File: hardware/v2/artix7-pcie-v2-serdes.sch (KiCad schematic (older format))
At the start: 22 parts, among them J4 USB3_A, J5 USB3_A, U1 XC7A75T-FGG484

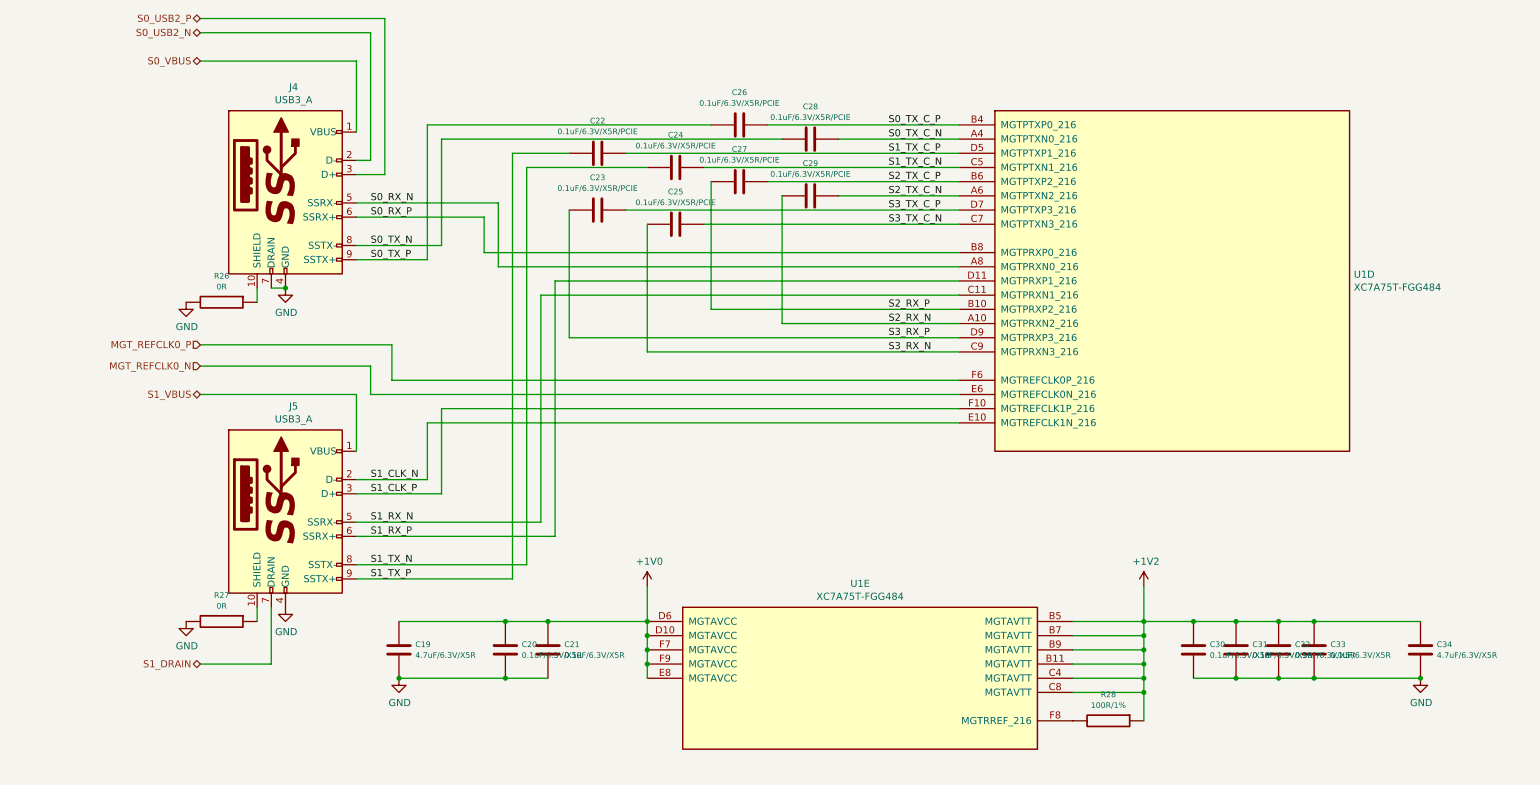
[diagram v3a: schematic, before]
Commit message: v2 pcb/schematic update : drc passing, need to add caps
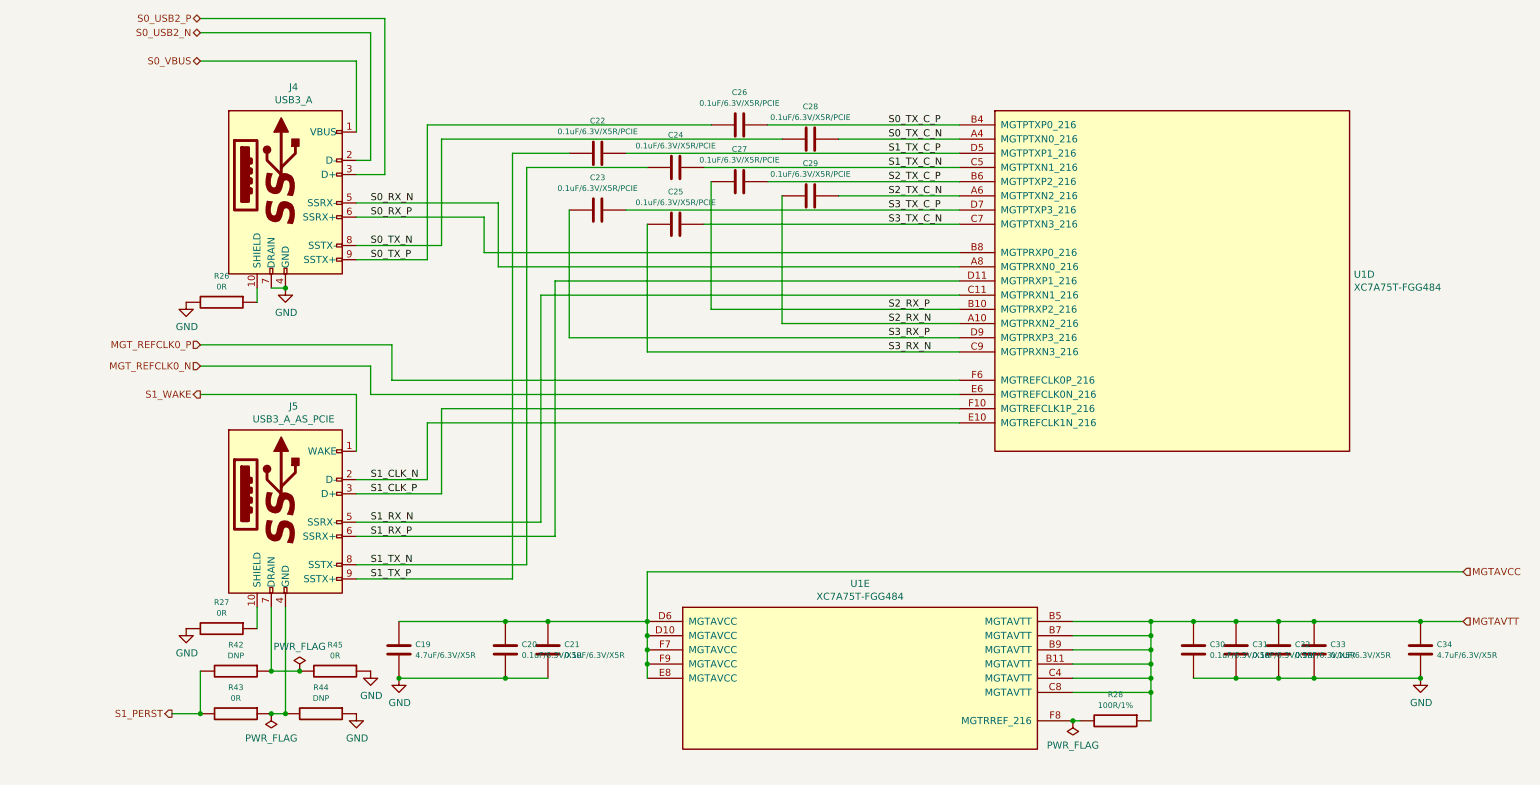
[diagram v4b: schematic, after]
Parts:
- removed J5: USB3_A, tom-connectors:USB3_A_Aliexpress, symbol tom-connectors:USB3_A
- added J5: USB3_A_AS_PCIE, tom-connectors:USB3_A_Aliexpress, symbol tom-connectors:USB3_A_AS_PCIE
- added R42, R44: DNP, tom-passives:C_0402_1005Metric, symbol tom-passives:R
- added R43, R45: 0R, tom-passives:C_0402_1005Metric, symbol tom-passives:R
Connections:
- net GND: now also R44.1, R45.1
- net S1_CLK_N: now also J5.2 (D-)
- net S1_CLK_P: now also J5.3 (D+)
- net S1_RX_N: now also J5.5 (SSRX-)
- net S1_RX_P: now also J5.6 (SSRX+)
- net S1_TX_N: now also J5.8 (SSTX-)
- net S1_TX_P: now also J5.9 (SSTX+)
- net at R27.1: now also J5.10 (SHIELD)
- net +1V0 renamed MGTAVCC
- net +1V2 renamed MGTAVTT
- new net: J5.4 (GND), R43.1, R44.2
- new net: J5.7 (DRAIN), R42.1, R45.2
- new net S1_PERST: R42.2, R43.2
- new net S1_WAKE: J5.1 (WAKE)
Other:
- moved on the sheet: R27, R28
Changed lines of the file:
@@
 EESchema Schematic File Version 4
-LIBS:artix7-pcie-v2-cache
 EELAYER 30 0
 EELAYER END
 $Descr A4 11693 8268
 encoding utf-8
-Sheet 4 7
+Sheet 2 7
 Title ""
 Date ""
@@
 	1    0    0    -1
 $EndComp
-Text HLabel 1900 5600 0    50   BiDi ~ 0
-S1_DRAIN
-Wire Wire Line
-	2400 5600 1900 5600
-Wire Wire Line
-	2400 5200 2400 5600
-Wire Wire Line
-	2300 5200 2300 5300
+Text HLabel 1700 5950 0    50   Output ~ 0
+S1_PERST
+Wire Wire Line
+	2300 5200 2300 5350
 $Comp
 L power:GND #PWR059
 U 1 1 5EAD2F17
-P 1800 5300
-F 0 "#PWR059" H 1800 5050 50  0001 C CNN
-F 1 "GND" H 1805 5127 50  0000 C CNN
-F 2 "" H 1800 5300 50  0001 C CNN
-F 3 "" H 1800 5300 50  0001 C CNN
-	1    1800 5300
+P 1800 5350
+F 0 "#PWR059" H 1800 5100 50  0001 C CNN
+F 1 "GND" H 1805 5177 50  0000 C CNN
+F 2 "" H 1800 5350 50  0001 C CNN
+F 3 "" H 1800 5350 50  0001 C CNN
+	1    1800 5350
 	1    0    0    -1
 $EndComp
@@
 L tom-passives:R R27
 U 1 1 5EAD1FF6
-P 2050 5300
-F 0 "R27" V 1865 5300 40  0000 C CNN
-F 1 "0R" V 1941 5300 40  0000 C CNN
-F 2 "tom-passives:C_0402_1005Metric" V 1980 5300 30  0001 C CNN
-F 3 "" H 2050 5300 30  0001 C CNN
-	1    2050 5300
+P 2050 5350
+F 0 "R27" V 1865 5350 40  0000 C CNN
+F 1 "0R" V 1941 5350 40  0000 C CNN
+F 2 "tom-passives:C_0402_1005Metric" V 1980 5350 30  0001 C CNN
+F 3 "" H 2050 5350 30  0001 C CNN
+	1    2050 5350
 	0    1    1    0
 $EndComp
@@
 L power:GND #PWR061
 U 1 1 5EACBD31
-P 2500 5200
-F 0 "#PWR061" H 2500 4950 50  0001 C CNN
-F 1 "GND" H 2505 5027 50  0000 C CNN
-F 2 "" H 2500 5200 50  0001 C CNN
-F 3 "" H 2500 5200 50  0001 C CNN
-	1    2500 5200
+P 3000 5950
+F 0 "#PWR061" H 3000 5700 50  0001 C CNN
+F 1 "GND" H 3005 5777 50  0000 C CNN
+F 2 "" H 3000 5950 50  0001 C CNN
+F 3 "" H 3000 5950 50  0001 C CNN
+	1    3000 5950
 	1    0    0    -1
 $EndComp
@@
 Wire Wire Line
 	3000 4600 4300 4600
-$Comp
-L tom-connectors:USB3_A J5
-U 1 1 5E9A32AC
-P 2500 4500
-F 0 "J5" H 2557 5217 50  0000 C CNN
-F 1 "USB3_A" H 2557 5126 50  0000 C CNN
-F 2 "tom-connectors:USB3_A_Aliexpress" H 2650 4600 50  0001 C CNN
-F 3 "~" H 2650 4600 50  0001 C CNN
-	1    2500 4500
-	1    0    0    -1
-$EndComp
 Wire Wire Line
 	7250 3800 3600 3800
@@
 Text Label 3100 5000 0    50   ~ 0
 S1_TX_P
-Text HLabel 1900 1350 0    50   BiDi ~ 0
-S0_VBUS
 Wire Wire Line
 	3000 1850 3000 1350
 Wire Wire Line
 	3000 1350 1900 1350
-Text HLabel 1900 3700 0    50   BiDi ~ 0
-S1_VBUS
+Text HLabel 1900 3700 0    50   Output ~ 0
+S1_WAKE
 Wire Wire Line
 	3000 4100 3000 3700
@@
 L tom-passives:R R28
 U 1 1 5EB72E9F
-P 8300 6000
-F 0 "R28" V 8115 6000 40  0000 C CNN
-F 1 "100R/1%" V 8191 6000 40  0000 C CNN
-F 2 "tom-passives:C_0402_1005Metric" V 8230 6000 30  0001 C CNN
-F 3 "" H 8300 6000 30  0001 C CNN
-	1    8300 6000
-	0    1    1    0
-$EndComp
-$Comp
-L power:+1V2 #PWR064
-U 1 1 5EB7A45C
-P 8550 5050
-F 0 "#PWR064" H 8550 4900 50  0001 C CNN
-F 1 "+1V2" H 8565 5223 50  0000 C CNN
-F 2 "" H 8550 5050 50  0001 C CNN
-F 3 "" H 8550 5050 50  0001 C CNN
-	1    8550 5050
-	1    0    0    -1
-$EndComp
-Wire Wire Line
-	8050 5300 8550 5300
-Wire Wire Line
-	8550 5050 8550 5300
-Connection ~ 8550 5300
-Wire Wire Line
-	8550 5300 8550 5400
-Wire Wire Line
-	8050 5400 8550 5400
-Connection ~ 8550 5400
-Wire Wire Line
-	8050 5500 8550 5500
-Wire Wire Line
-	8550 5400 8550 5500
-Connection ~ 8550 5500
-Wire Wire Line
-	8550 5500 8550 5600
-Wire Wire Line
-	8050 5600 8550 5600
-Connection ~ 8550 5600
-Wire Wire Line
-	8550 5600 8550 5700
-Wire Wire Line
-	8050 5700 8550 5700
-Connection ~ 8550 5700
-Wire Wire Line
-	8550 5700 8550 5800
-Wire Wire Line
-	8050 5800 8550 5800
-Connection ~ 8550 5800
-Wire Wire Line
-	8550 5800 8550 6000
+P 8350 6000
+F 0 "R28" V 8165 6000 40  0000 C CNN
+F 1 "100R/1%" V 8241 6000 40  0000 C CNN
+F 2 "tom-passives:C_0402_1005Metric" V 8280 6000 30  0001 C CNN
+F 3 "" H 8350 6000 30  0001 C CNN
+	1    8350 6000
+	0    1    1    0
+$EndComp
+Wire Wire Line
+	8050 5300 8600 5300
+Connection ~ 8600 5300
+Wire Wire Line
+	8600 5300 8600 5400
+Wire Wire Line
+	8050 5400 8600 5400
+Connection ~ 8600 5400
+Wire Wire Line
+	8050 5500 8600 5500
+Wire Wire Line
+	8600 5400 8600 5500
+Connection ~ 8600 5500
+Wire Wire Line
+	8600 5500 8600 5600
+Wire Wire Line
+	8050 5600 8600 5600
+Connection ~ 8600 5600
+Wire Wire Line
+	8600 5600 8600 5700
+Wire Wire Line
+	8050 5700 8600 5700
+Connection ~ 8600 5700
+Wire Wire Line
+	8600 5700 8600 5800
+Wire Wire Line
+	8050 5800 8600 5800
 $Comp
 L tom-passives:C C30
@@
 $EndComp
 Wire Wire Line
-	8550 5300 8900 5300
+	8600 5300 8900 5300
 Connection ~ 8900 5300
 Wire Wire Line
@@
 Wire Wire Line
 	8900 5700 9200 5700
-$Comp
-L power:+1V0 #PWR063
-U 1 1 5EBF7D68
-P 5050 5050
-F 0 "#PWR063" H 5050 4900 50  0001 C CNN
-F 1 "+1V0" H 5065 5223 50  0000 C CNN
-F 2 "" H 5050 5050 50  0001 C CNN
-F 3 "" H 5050 5050 50  0001 C CNN
-	1    5050 5050
-	1    0    0    -1
-$EndComp
 Wire Wire Line
 	5050 5700 5050 5600
 Connection ~ 5050 5300
-Wire Wire Line
-	5050 5300 5050 5050
 Connection ~ 5050 5400
 Wire Wire Line
@@
 Text HLabel 1900 3350 0    50   Input ~ 0
 MGT_REFCLK0_P
+Text HLabel 10800 5300 2    50   Input ~ 0
+MGTAVTT
+Wire Wire Line
+	10800 5300 10500 5300
+Connection ~ 10500 5300
+Text HLabel 10800 4950 2    50   Input ~ 0
+MGTAVCC
+Wire Wire Line
+	10800 4950 5050 4950
+Wire Wire Line
+	5050 4950 5050 5300
+Wire Wire Line
+	8600 5800 8600 6000
+Connection ~ 8600 5800
+Wire Wire Line
+	8100 6000 8050 6000
+$Comp
+L power:PWR_FLAG #FLG0112
+U 1 1 5EE50010
+P 8050 6000
+F 0 "#FLG0112" H 8050 6075 50  0001 C CNN
+F 1 "PWR_FLAG" H 8050 6173 50  0000 C CNN
+F 2 "" H 8050 6000 50  0001 C CNN
+F 3 "~" H 8050 6000 50  0001 C CNN
+	1    8050 6000
+	-1   0    0    1
+$EndComp
+Connection ~ 8050 6000
+Text HLabel 1900 1350 0    50   BiDi ~ 0
+S0_VBUS
+$Comp
+L tom-connectors:USB3_A_AS_PCIE J5
+U 1 1 5EEEB708
+P 2500 4500
+F 0 "J5" H 2557 5217 50  0000 C CNN
+F 1 "USB3_A_AS_PCIE" H 2557 5126 50  0000 C CNN
+F 2 "tom-connectors:USB3_A_Aliexpress" H 2650 4600 50  0001 C CNN
+F 3 "~" H 2650 4600 50  0001 C CNN
+	1    2500 4500
+	1    0    0    -1
+$EndComp
+$Comp
+L tom-passives:R R44
+U 1 1 5F029E9A
+P 2750 5950
+F 0 "R44" V 2565 5950 40  0000 C CNN
+F 1 "DNP" V 2641 5950 40  0000 C CNN
+F 2 "tom-passives:C_0402_1005Metric" V 2680 5950 30  0001 C CNN
+F 3 "" H 2750 5950 30  0001 C CNN
+	1    2750 5950
+	0    1    1    0
+$EndComp
+$Comp
+L tom-passives:R R43
+U 1 1 5F02A201
+P 2150 5950
+F 0 "R43" V 1965 5950 40  0000 C CNN
+F 1 "0R" V 2041 5950 40  0000 C CNN
+F 2 "tom-passives:C_0402_1005Metric" V 2080 5950 30  0001 C CNN
+F 3 "" H 2150 5950 30  0001 C CNN
+	1    2150 5950
+	0    1    1    0
+$EndComp
+Wire Wire Line
+	2500 5200 2500 5950
+Wire Wire Line
+	2500 5950 2400 5950
+Connection ~ 2500 5950
+Wire Wire Line
+	1700 5950 1900 5950
+$Comp
+L tom-passives:R R42
+U 1 1 5F0598E8
+P 2150 5650
+F 0 "R42" V 1965 5650 40  0000 C CNN
+F 1 "DNP" V 2041 5650 40  0000 C CNN
+F 2 "tom-passives:C_0402_1005Metric" V 2080 5650 30  0001 C CNN
+F 3 "" H 2150 5650 30  0001 C CNN
+	1    2150 5650
+	0    1    1    0
+$EndComp
+Wire Wire Line
+	1900 5650 1900 5950
+Connection ~ 1900 5950
+Wire Wire Line
+	2400 5200 2400 5650
+$Comp
+L tom-passives:R R45
+U 1 1 5F07398D
+P 2850 5650
+F 0 "R45" V 2665 5650 40  0000 C CNN
+F 1 "0R" V 2741 5650 40  0000 C CNN
+F 2 "tom-passives:C_0402_1005Metric" V 2780 5650 30  0001 C CNN
+F 3 "" H 2850 5650 30  0001 C CNN
+	1    2850 5650
+	0    1    1    0
+$EndComp
+$Comp
+L power:GND #PWR035
+U 1 1 5F073E12
+P 3100 5650
+F 0 "#PWR035" H 3100 5400 50  0001 C CNN
+F 1 "GND" H 3105 5477 50  0000 C CNN
+F 2 "" H 3100 5650 50  0001 C CNN
+F 3 "" H 3100 5650 50  0001 C CNN
+	1    3100 5650
+	1    0    0    -1
+$EndComp
+Wire Wire Line
+	2600 5650 2400 5650
+Connection ~ 2400 5650
+$Comp
+L power:PWR_FLAG #FLG0114
+U 1 1 5F118316
+P 2600 5650
+F 0 "#FLG0114" H 2600 5725 50  0001 C CNN
+F 1 "PWR_FLAG" H 2600 5823 50  0000 C CNN
+F 2 "" H 2600 5650 50  0001 C CNN
+F 3 "~" H 2600 5650 50  0001 C CNN
+	1    2600 5650
+	1    0    0    -1
+$EndComp
+Connection ~ 2600 5650
+$Comp
+L power:PWR_FLAG #FLG0115
+U 1 1 5F11842A
+P 2400 5950
+F 0 "#FLG0115" H 2400 6025 50  0001 C CNN
+F 1 "PWR_FLAG" H 2400 6123 50  0000 C CNN
+F 2 "" H 2400 5950 50  0001 C CNN
+F 3 "~" H 2400 5950 50  0001 C CNN
+	1    2400 5950
+	-1   0    0    1
+$EndComp
+Connection ~ 2400 5950
 $EndSCHEMATC

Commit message: v2 hardware: pcb progress commit, 155 unrouted
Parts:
- removed C23, C25, C27, C29: 0.1uF/6.3V/X5R/PCIE, tom-passives:C_0402_1005Metric, symbol tom-passives:C
- removed C31: 0.1uF/6.3V/X5R, tom-passives:C_0402_1005Metric, symbol tom-passives:C
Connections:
- net S2_RX_N is gone; now on net GND: U1.A10 (MGTPRXN2_216)
- net S2_RX_P is gone; now on net GND: U1.B10 (MGTPRXP2_216)
- net GND: now also U1.C11 (MGTPRXN1_216), U1.D11 (MGTPRXP1_216)
- net MGTAVTT: now also R28.2; no longer R28.1
- net S3_RX_N: now also J5.5 (SSRX-)
- net S3_RX_P: now also J5.6 (SSRX+)
- net S3_TX_C_N: now also C24.1
- net S3_TX_C_P: now also C22.1
- net MGTRREF: now reaches U1.F8 (MGTRREF_216)
- net MGTRREF: now also R28.1; no longer R28.2
- net S1_CLK_N renamed S3_CLK_N
- net S1_CLK_P renamed S3_CLK_P
- net S1_PERST renamed S3_PERST
- removed net S1_RX_N: J5.5 (SSRX-), U1.C11 (MGTPRXN1_216)
- removed net S1_RX_P: J5.6 (SSRX+), U1.D11 (MGTPRXP1_216)
- net S1_TX_C_N: no longer names the net of U1.C5 (MGTPTXN1_216)
- net S1_TX_C_N: no longer C24.1
- net S1_TX_C_P: no longer names the net of U1.D5 (MGTPTXP1_216)
- net S1_TX_C_P: no longer C22.1
- net S1_TX_N renamed S3_TX_N
- net S1_TX_P renamed S3_TX_P
- net S1_WAKE renamed S3_WAKE
- net S2_TX_C_N: no longer names the net of U1.A6 (MGTPTXN2_216)
- net S2_TX_C_P: no longer names the net of U1.B6 (MGTPTXP2_216)
- no-connect marks 0 -> 4
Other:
- moved on the sheet: C22, C24, C32, C33, C34

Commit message: v2 pcb/schematic progress commit, all tough signals routed out
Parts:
- added C47, C48: 0.1uF/6.3V/X5R/PCIE, tom-passives:C_0402_1005Metric, symbol tom-passives:C
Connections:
- net GND: now also U1.C9 (MGTPRXN3_216), U1.D9 (MGTPRXP3_216); no longer U1.A10 (MGTPRXN2_216), U1.B10 (MGTPRXP2_216)
- net S2_TX_C_N: now reaches U1.A6 (MGTPTXN2_216)
- net S2_TX_C_N: now also C24.1
- net S2_TX_C_P: now reaches U1.B6 (MGTPTXP2_216)
- net S2_TX_C_P: now also C22.1
- net S2_GND: now reaches J5.4 (GND), R43.1, R44.2
- net S2_DRAIN: now reaches J5.7 (DRAIN), R42.1, R45.2
- net S3_CLK_N renamed MGTREFCLK1_C_N
- net MGTREFCLK1_C_N: now also C48.2; no longer U1.E10 (MGTREFCLK1N_216)
- net S3_CLK_P renamed MGTREFCLK1_C_P
- net MGTREFCLK1_C_P: now also C47.2; no longer U1.F10 (MGTREFCLK1P_216)
- net S3_PERST renamed S2_PERST
- net S3_RX_N renamed S2_RX_N
- net S2_RX_N: now also U1.A10 (MGTPRXN2_216); no longer U1.C9 (MGTPRXN3_216)
- net S3_RX_P renamed S2_RX_P
- net S2_RX_P: now also U1.B10 (MGTPRXP2_216); no longer U1.D9 (MGTPRXP3_216)
- net S3_TX_C_N: no longer names the net of U1.C7 (MGTPTXN3_216)
- net S3_TX_C_N: no longer C24.1
- net S3_TX_C_P: no longer names the net of U1.D7 (MGTPTXP3_216)
- net S3_TX_C_P: no longer C22.1
- net S3_TX_N renamed S2_TX_N
- net S3_TX_P renamed S2_TX_P
- net S3_WAKE renamed S2_WAKE
- new net MGTREFCLK1_N: C48.1, U1.E10 (MGTREFCLK1N_216)
- new net MGTREFCLK1_P: C47.1, U1.F10 (MGTREFCLK1P_216)
- no-connect marks 4 -> 2
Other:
- moved on the sheet: C22, C24
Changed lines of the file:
@@
 Wire Wire Line
 	3900 2700 7250 2700
-Wire Wire Line
-	4300 4600 4300 3400
 Text Label 3100 2350 0    50   ~ 0
 S0_RX_N
@@
 $EndComp
 Text HLabel 1700 5950 0    50   Output ~ 0
-S3_PERST
+S2_PERST
 Wire Wire Line
 	2300 5200 2300 5350
@@
 $EndComp
 Wire Wire Line
-	3000 4300 3500 4300
-Wire Wire Line
-	3000 4400 3600 4400
+	3000 4300 3900 4300
+Wire Wire Line
+	3000 4400 4000 4400
 Text Label 3100 4700 0    50   ~ 0
-S3_RX_P
+S2_RX_P
 Text Label 3100 4600 0    50   ~ 0
-S3_RX_N
+S2_RX_N
 Text Label 3100 4400 0    50   ~ 0
-S3_CLK_P
+MGTREFCLK1_C_P
 Text Label 3100 4300 0    50   ~ 0
-S3_CLK_N
-Wire Wire Line
-	3500 3900 7250 3900
-Wire Wire Line
-	3500 4300 3500 3900
-Wire Wire Line
-	4400 4700 3000 4700
+MGTREFCLK1_C_N
+Wire Wire Line
+	3900 3900 5450 3900
+Wire Wire Line
+	3900 4300 3900 3900
 Wire Wire Line
 	3000 4600 4300 4600
 Wire Wire Line
-	7250 3800 3600 3800
-Wire Wire Line
-	3600 3800 3600 4400
+	7250 3800 5350 3800
+Wire Wire Line
+	4000 3800 4000 4400
 Text Label 3100 4900 0    50   ~ 0
-S3_TX_N
+S2_TX_N
 Text Label 3100 5000 0    50   ~ 0
-S3_TX_P
+S2_TX_P
 Wire Wire Line
 	3000 1850 3000 1350
@@
 	3000 1350 1900 1350
 Text HLabel 1900 3700 0    50   Output ~ 0
-S3_WAKE
+S2_WAKE
 Wire Wire Line
 	3000 4100 3000 3700
@@
 L tom-passives:C C22
 U 1 1 5E746FE8
-P 4700 2400
-F 0 "C22" V 4471 2400 40  0000 C CNN
-F 1 "0.1uF/6.3V/X5R/PCIE" V 4547 2400 40  0000 C CNN
-F 2 "tom-passives:C_0402_1005Metric" H 4738 2250 30  0001 C CNN
-F 3 "" H 4700 2400 60  0001 C CNN
-	1    4700 2400
+P 4700 2200
+F 0 "C22" V 4471 2200 40  0000 C CNN
+F 1 "0.1uF/6.3V/X5R/PCIE" V 4547 2200 40  0000 C CNN
+F 2 "tom-passives:C_0402_1005Metric" H 4738 2050 30  0001 C CNN
+F 3 "" H 4700 2200 60  0001 C CNN
+	1    4700 2200
 	0    1    1    0
 $EndComp
@@
 L tom-passives:C C24
 U 1 1 5E7489FC
-P 5200 2500
-F 0 "C24" V 4971 2500 40  0000 C CNN
-F 1 "0.1uF/6.3V/X5R/PCIE" V 5047 2500 40  0000 C CNN
-F 2 "tom-passives:C_0402_1005Metric" H 5238 2350 30  0001 C CNN
-F 3 "" H 5200 2500 60  0001 C CNN
-	1    5200 2500
-	0    1    1    0
-$EndComp
-Wire Wire Line
-	4400 3300 4400 4700
+P 5200 2300
+F 0 "C24" V 4971 2300 40  0000 C CNN
+F 1 "0.1uF/6.3V/X5R/PCIE" V 5047 2300 40  0000 C CNN
+F 2 "tom-passives:C_0402_1005Metric" H 5238 2150 30  0001 C CNN
+F 3 "" H 5200 2300 60  0001 C CNN
+	1    5200 2300
+	0    1    1    0
+$EndComp
 Wire Wire Line
 	4000 2800 4000 2350
@@
 	4000 2800 7250 2800
 Wire Wire Line
-	4500 2400 4100 2400
-Wire Wire Line
-	4100 2400 4100 5000
+	4500 2200 4100 2200
 Wire Wire Line
 	4100 5000 3000 5000
@@
 	3000 4900 4200 4900
 Wire Wire Line
-	4200 4900 4200 2500
-Wire Wire Line
-	4200 2500 5000 2500
+	4200 2300 5000 2300
 Wire Wire Line
 	2400 2950 2500 2950
@@
 Text Label 6750 1800 0    50   ~ 0
 S0_TX_C_P
-Text Label 6750 2400 0    50   ~ 0
-S3_TX_C_P
-Text Label 6750 2500 0    50   ~ 0
-S3_TX_C_N
+Text Label 6750 2200 0    50   ~ 0
+S2_TX_C_P
+Text Label 6750 2300 0    50   ~ 0
+S2_TX_C_N
 Text HLabel 1900 3500 0    50   Input ~ 0
 MGT_REFCLK0_N
@@
 	3100 3700 3100 3500
 Wire Wire Line
-	3100 3500 1900 3500
-Wire Wire Line
 	7250 3600 3250 3600
 Wire Wire Line
 	3250 3600 3250 3350
-Wire Wire Line
-	3250 3350 1900 3350
 Text HLabel 1900 3350 0    50   Input ~ 0
 MGT_REFCLK0_P
@@
 P 2600 5650
 F 0 "#FLG0114" H 2600 5725 50  0001 C CNN
-F 1 "PWR_FLAG" H 2600 5823 50  0000 C CNN
+F 1 "PWR_FLAG" V 2600 5950 50  0000 C CNN
 F 2 "" H 2600 5650 50  0001 C CNN
 F 3 "~" H 2600 5650 50  0001 C CNN
@@
 NoConn ~ 7250 2100
 Wire Wire Line
-	4300 3400 7250 3400
-Wire Wire Line
-	7250 3300 4400 3300
-Wire Wire Line
-	7250 2500 5400 2500
-Wire Wire Line
-	4900 2400 7250 2400
-NoConn ~ 7250 2200
-NoConn ~ 7250 2300
+	4300 3200 7250 3200
+Wire Wire Line
+	7250 3100 4400 3100
+Wire Wire Line
+	7250 2300 5400 2300
+Wire Wire Line
+	4900 2200 7250 2200
 Wire Wire Line
 	7250 2900 7150 2900
@@
 Connection ~ 7150 3000
 Wire Wire Line
-	7150 3000 7150 3100
-Wire Wire Line
-	7150 3100 7250 3100
-Connection ~ 7150 3100
-Wire Wire Line
-	7150 3100 7150 3200
-Wire Wire Line
-	7250 3200 7150 3200
-Connection ~ 7150 3200
-Wire Wire Line
-	7150 3200 7150 4000
-Wire Wire Line
 	8050 6000 8050 6150
 Text Label 8050 6150 0    50   ~ 0
@@
 Wire Wire Line
 	8900 5700 9100 5700
+Text Label 2500 5600 1    50   ~ 0
+S2_GND
+Text Label 2400 5600 1    50   ~ 0
+S2_DRAIN
+Wire Wire Line
+	3100 3500 1900 3500
+Wire Wire Line
+	3250 3350 1900 3350
+$Comp
+L tom-passives:C C48
+U 1 1 5EDACCD3
+P 5650 3900
+F 0 "C48" V 5421 3900 40  0000 C CNN
+F 1 "0.1uF/6.3V/X5R/PCIE" V 5497 3900 40  0000 C CNN
+F 2 "tom-passives:C_0402_1005Metric" H 5688 3750 30  0001 C CNN
+F 3 "" H 5650 3900 60  0001 C CNN
+	1    5650 3900
+	0    1    -1   0
+$EndComp
+Wire Wire Line
+	5850 3900 7250 3900
+$Comp
+L tom-passives:C C47
+U 1 1 5EDAF2BE
+P 5150 3800
+F 0 "C47" V 4921 3800 40  0000 C CNN
+F 1 "0.1uF/6.3V/X5R/PCIE" V 4997 3800 40  0000 C CNN
+F 2 "tom-passives:C_0402_1005Metric" H 5188 3650 30  0001 C CNN
+F 3 "" H 5150 3800 60  0001 C CNN
+	1    5150 3800
+	0    1    -1   0
+$EndComp
+Wire Wire Line
+	4950 3800 4000 3800
+Text Label 6250 3900 0    50   ~ 0
+MGTREFCLK1_N
+Text Label 6250 3800 0    50   ~ 0
+MGTREFCLK1_P
+Wire Wire Line
+	3000 4700 4400 4700
+Wire Wire Line
+	4100 2200 4100 5000
+Wire Wire Line
+	4200 4900 4200 2300
+Wire Wire Line
+	7150 3000 7150 3300
+Wire Wire Line
+	4300 3200 4300 4600
+Wire Wire Line
+	4400 3100 4400 4700
+Wire Wire Line
+	7250 3300 7150 3300
+Connection ~ 7150 3300
+Wire Wire Line
+	7150 3300 7150 3400
+Wire Wire Line
+	7250 3400 7150 3400
+Connection ~ 7150 3400
+Wire Wire Line
+	7150 3400 7150 4000
 $EndSCHEMATC
